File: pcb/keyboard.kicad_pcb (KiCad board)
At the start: 2 copper layers, 92.9 x 61.9 mm, 24 parts, among them U1 Arduino_Pro_Micro

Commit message: Modified KiCad hardware files
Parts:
- removed ? (x4): , 
- removed U1: Arduino_Pro_Micro, ScottoKeebs_MCU:Arduino_Pro_Micro
- added A1: RaspberryPi_Pico, Module:RaspberryPi_Pico_Common_Unspecified, F.Cu at (147.0, 72.1)
- added REF**: MountingHole_2.2mm_M2, MountingHole:MountingHole_2.2mm_M2, F.Cu at (64.3, 50.0)
- added REF**: MountingHole_2.2mm_M2, MountingHole:MountingHole_2.2mm_M2, F.Cu at (64.3, 107.2)
- added REF**: MountingHole_2.2mm_M2, MountingHole:MountingHole_2.2mm_M2, F.Cu at (161.9, 50.0)
- moved REF** 12.8 mm to (161.9, 107.2)
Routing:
- net Row 2: track 73.5 -> 87.0 mm
- net Row 1: track 56.6 -> 69.7 mm
- net col 0: track 121.1 -> 108.7 mm
- net col 2: track 76.2 -> 66.1 mm
- net col 1: track 95.3 -> 88.7 mm
- net Row 0: track 52.0 -> 52.8 mm
- removed copper zone on B.Cu, net (none)
- removed copper zone on F.Cu, net (none)
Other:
- board size 92.9 x 61.9 mm -> 106.9 x 64.7 mm
- board text added: "Front side"
- board text added: "MX-style Switches"
- board text added: "Rasspberry pi_Pico"
- board text removed: "This side Back"
- board text removed: "This side front"
- board text removed: "credits jagrit"
- board text removed: "↑ Arduino Pro Micro"
- board text removed: "↑ MX-style switches"

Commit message: oled screen a dial new case new pc
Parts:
- removed A1: RaspberryPi_Pico, Module:RaspberryPi_Pico_Common_Unspecified
- removed the REF** at (64.3, 50.0)
- removed the REF** at (161.9, 107.2)
- removed the REF** at (64.3, 107.2)
- removed the REF** at (161.9, 50.0)
- added J1: Conn_01x04_Pin, Display:ER_OLEDM0.91_1x-I2C, F.Cu at (85.0, 56.0)
- added REF**: ToolingHole_1.152mm, MountingHole:ToolingHole_1.152mm, F.Cu at (87.7, 68.0)
- added REF**: ToolingHole_1.152mm, MountingHole:ToolingHole_1.152mm, F.Cu at (46.0, 127.6)
- added REF**: ToolingHole_1.152mm, MountingHole:ToolingHole_1.152mm, F.Cu at (108.5, 127.6)
- added REF**: ToolingHole_1.152mm, MountingHole:ToolingHole_1.152mm, F.Cu at (45.4, 50.8)
- added SW1: RotaryEncoder_Switch, Rotary_Encoder:RotaryEncoder_Alps_EC11E-Switch_Vertical_H20mm, F.Cu at (90.7, 57.1)
- added U1: MCU_Seeed_XIAO_RP2040, ScottoKeebs_MCU:Seeed_XIAO_RP2040, B.Cu at (58.7, 59.7)
- D1, D2, D3, D4, D5, D6, D7, D8, D9: moved to F.Cu
- moved S1 30.8 mm to (57.0, 81.3)
- moved D5 30.8 mm to (85.6, 104.1)
- moved D6 30.8 mm to (104.6, 104.1)
- moved D8 30.8 mm to (85.6, 123.2)
- moved D9 30.8 mm to (104.6, 123.2)
- moved S2 30.8 mm to (76.0, 81.3)
- moved S3 30.8 mm to (95.1, 81.3)
- moved D4 30.8 mm to (66.5, 104.1)
- moved D7 30.8 mm to (66.5, 123.2)
- moved S4 30.8 mm to (57.0, 100.3)
- moved S5 30.8 mm to (76.0, 100.3)
- moved S6 30.8 mm to (95.1, 100.3)
- moved S7 30.8 mm to (57.0, 119.4)
- moved S8 30.8 mm to (76.0, 119.4)
- moved S9 30.8 mm to (95.1, 119.4)
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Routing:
- net ENC_A: track 0.00 -> 126.0 mm
- net ENC_B: track 0.00 -> 113.9 mm
- net col 2: track 66.1 -> 152.2 mm
- net Row 2: track 87.0 -> 169.2 mm
- net ENC_SW: track 0.00 -> 81.9 mm
- net Row 1: track 69.7 -> 143.9 mm
- net Row 0: track 52.8 -> 114.8 mm
- net 3V3: track 0.00 -> 57.7 mm
- net col 0: track 108.7 -> 62.7 mm
- net col 1: track 88.7 -> 51.7 mm
- net SCL: track 0.00 -> 24.3 mm
- net SDA: track 0.00 -> 19.2 mm
- net GND: track 0.00 -> 13.1 mm, vias 0 -> 4
- net Net-(D2-A): track 7.51 -> 6.80 mm
- net Net-(D3-A): track 7.51 -> 6.86 mm
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- added copper zone on B.Cu, net GND
- added copper zone on F.Cu, net GND
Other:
- board size 106.9 x 64.7 mm -> 66.4 x 81.9 mm
- board text added: "Credits ~jagrit"
- board text added: "GND"
- board text added: "MX-Styles Keys"
- board text added: "OLED Display"
- board text added: "Place here"
- board text added: "Rotary Encoder"
- board text added: "isn't is cool?"
- board text added: "this is project took 15-20hrs"
- board text added: "xiao rp2040"
- board text removed: "Front side"
- board text removed: "MX-style Switches"
- board text removed: "Rasspberry pi_Pico"
- board text removed: "this is micropad"

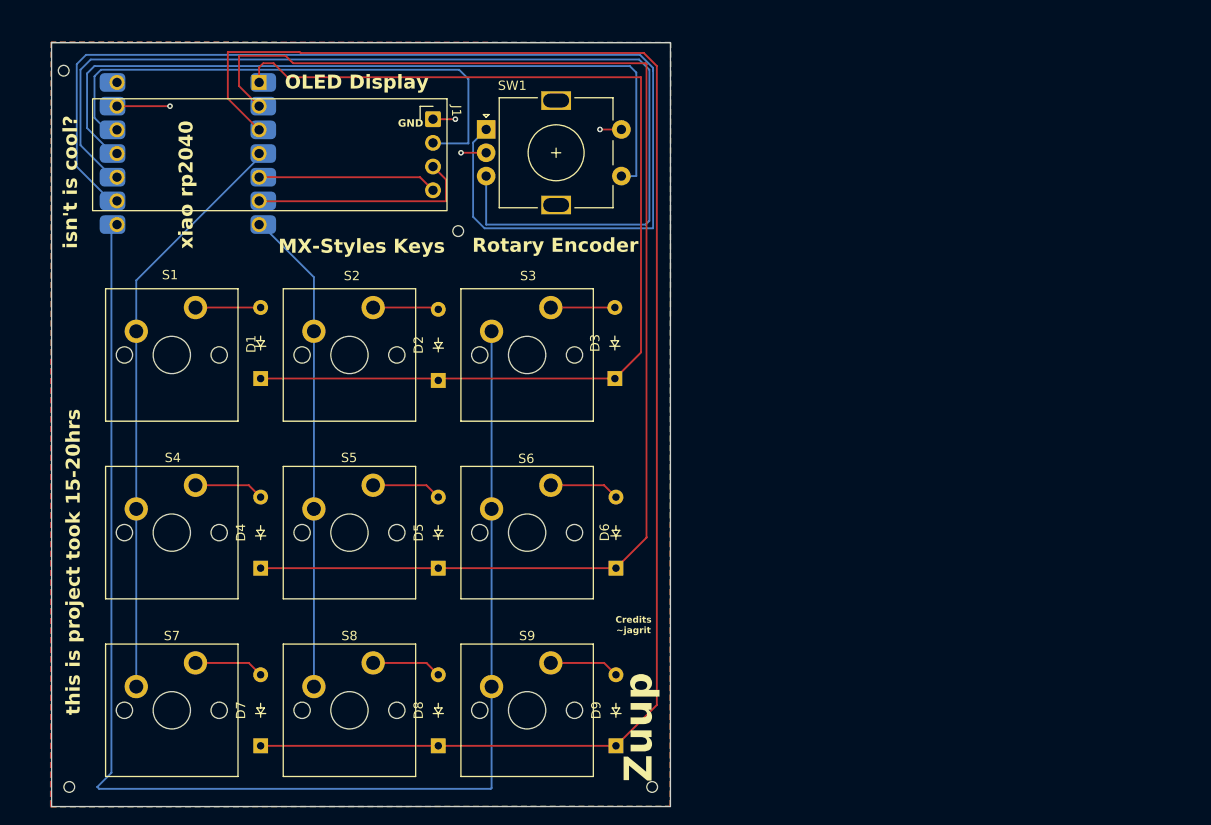
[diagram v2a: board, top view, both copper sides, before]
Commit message: clean repo remove large file
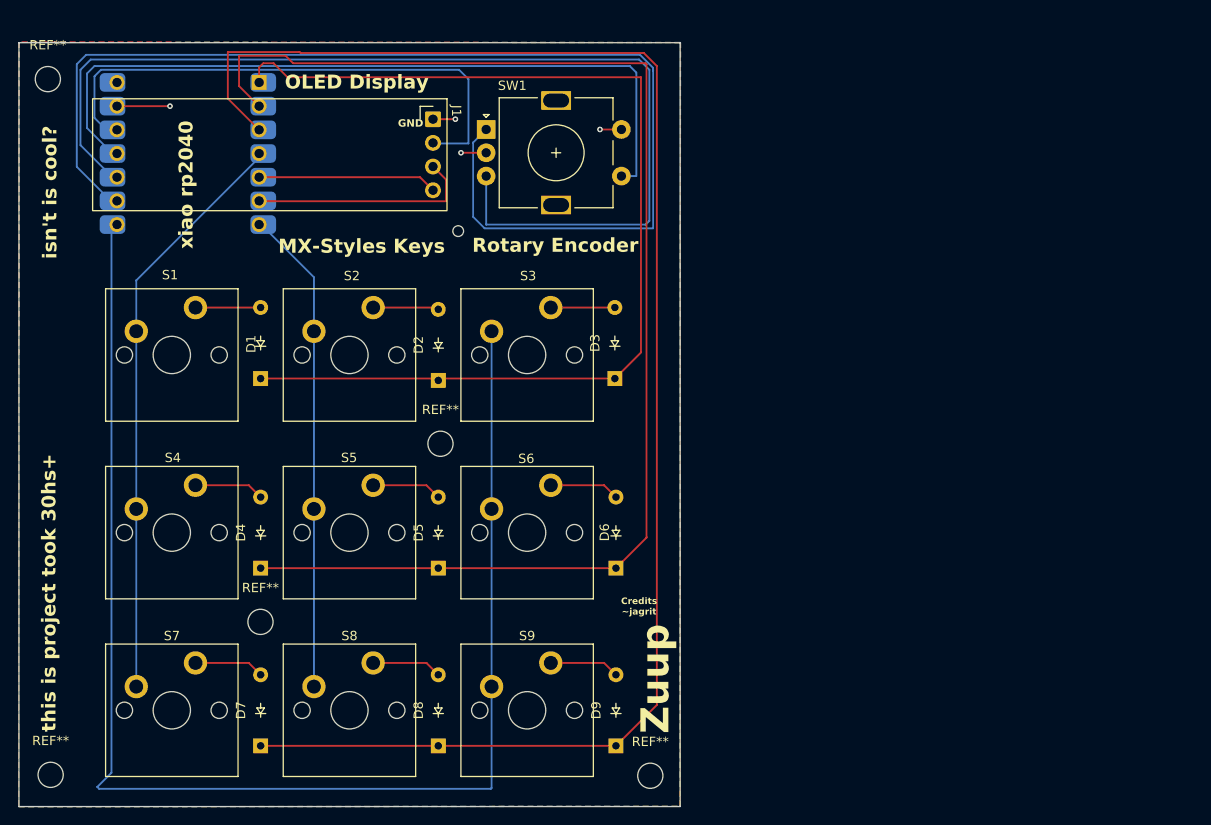
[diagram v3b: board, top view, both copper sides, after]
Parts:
- removed the REF** at (46.0, 127.6)
- removed the REF** at (108.5, 127.6)
- removed the REF** at (45.4, 50.8)
- added REF**: MountingHole_2.7mm_M2.5, MountingHole:MountingHole_2.7mm_M2.5, F.Cu at (85.8, 90.8)
- added REF**: MountingHole_2.7mm_M2.5, MountingHole:MountingHole_2.7mm_M2.5, F.Cu at (108.3, 126.4)
- added REF**: MountingHole_2.7mm_M2.5, MountingHole:MountingHole_2.7mm_M2.5, F.Cu at (43.7, 51.7)
- added REF**: MountingHole_2.7mm_M2.5, MountingHole:MountingHole_2.7mm_M2.5, F.Cu at (44.0, 126.3)
- added REF**: MountingHole_2.7mm_M2.5, MountingHole:MountingHole_2.7mm_M2.5, F.Cu at (66.5, 109.9)
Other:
- board size 66.4 x 81.9 mm -> 70.9 x 81.9 mm
- board text added: "this is project took 30hs+"
- board text removed: "this is project took 15-20hrs"
